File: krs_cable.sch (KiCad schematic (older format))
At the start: 0 parts

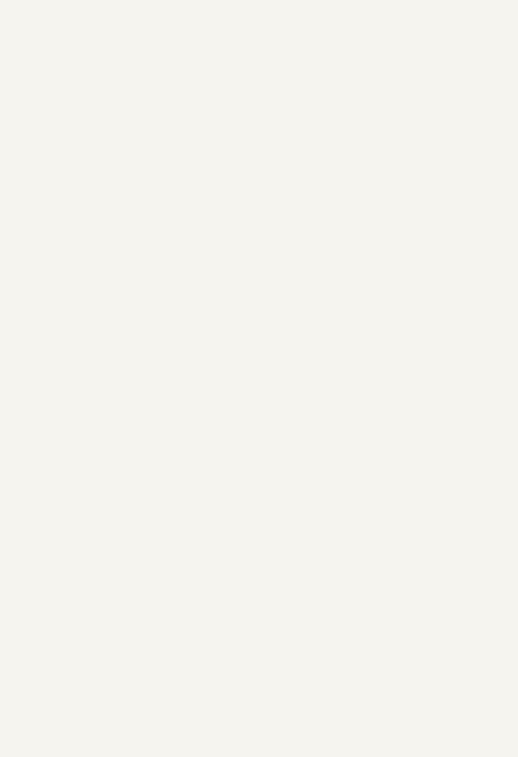
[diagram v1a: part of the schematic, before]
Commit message: set limits to pull down, optional invert
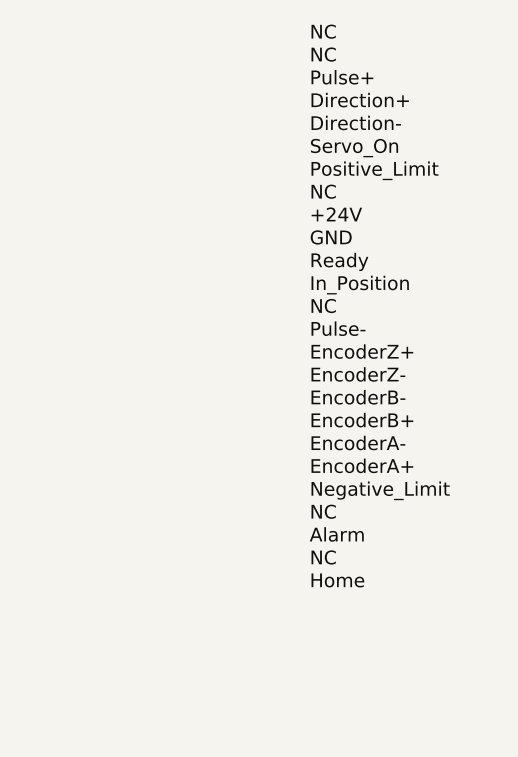
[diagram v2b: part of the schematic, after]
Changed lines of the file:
@@
 Text HLabel 4700 6500 3    60   Input ~ 0
 X2+24V
+Text Label 9000 1200 0    60   ~ 0
+NC
+Text Label 9000 1300 0    60   ~ 0
+NC
+Text Label 9000 1400 0    60   ~ 0
+Pulse+
+Text Label 9000 1500 0    60   ~ 0
+Direction+
+Text Label 9000 1600 0    60   ~ 0
+Direction-
+Text Label 9000 1700 0    60   ~ 0
+Servo_On
+Text Label 9000 1800 0    60   ~ 0
+Positive_Limit
+Text Label 9000 1900 0    60   ~ 0
+NC
+Text Label 9000 2000 0    60   ~ 0
++24V
+Text Label 9000 2100 0    60   ~ 0
+GND
+Text Label 9000 2200 0    60   ~ 0
+Ready
+Text Label 9000 2300 0    60   ~ 0
+In_Position
+Text Label 9000 2400 0    60   ~ 0
+NC
+Text Label 9000 2500 0    60   ~ 0
+Pulse-
+Text Label 9000 2600 0    60   ~ 0
+EncoderZ+
+Text Label 9000 2700 0    60   ~ 0
+EncoderZ-
+Text Label 9000 2800 0    60   ~ 0
+EncoderB-
+Text Label 9000 3000 0    60   ~ 0
+EncoderA-
+Text Label 9000 2900 0    60   ~ 0
+EncoderB+
+Text Label 9000 3100 0    60   ~ 0
+EncoderA+
+Text Label 9000 3200 0    60   ~ 0
+Negative_Limit
+Text Label 9000 3300 0    60   ~ 0
+NC
+Text Label 9000 3400 0    60   ~ 0
+Alarm
+Text Label 9000 3500 0    60   ~ 0
+NC
+Text Label 9000 3600 0    60   ~ 0
+Home
 $EndSCHEMATC

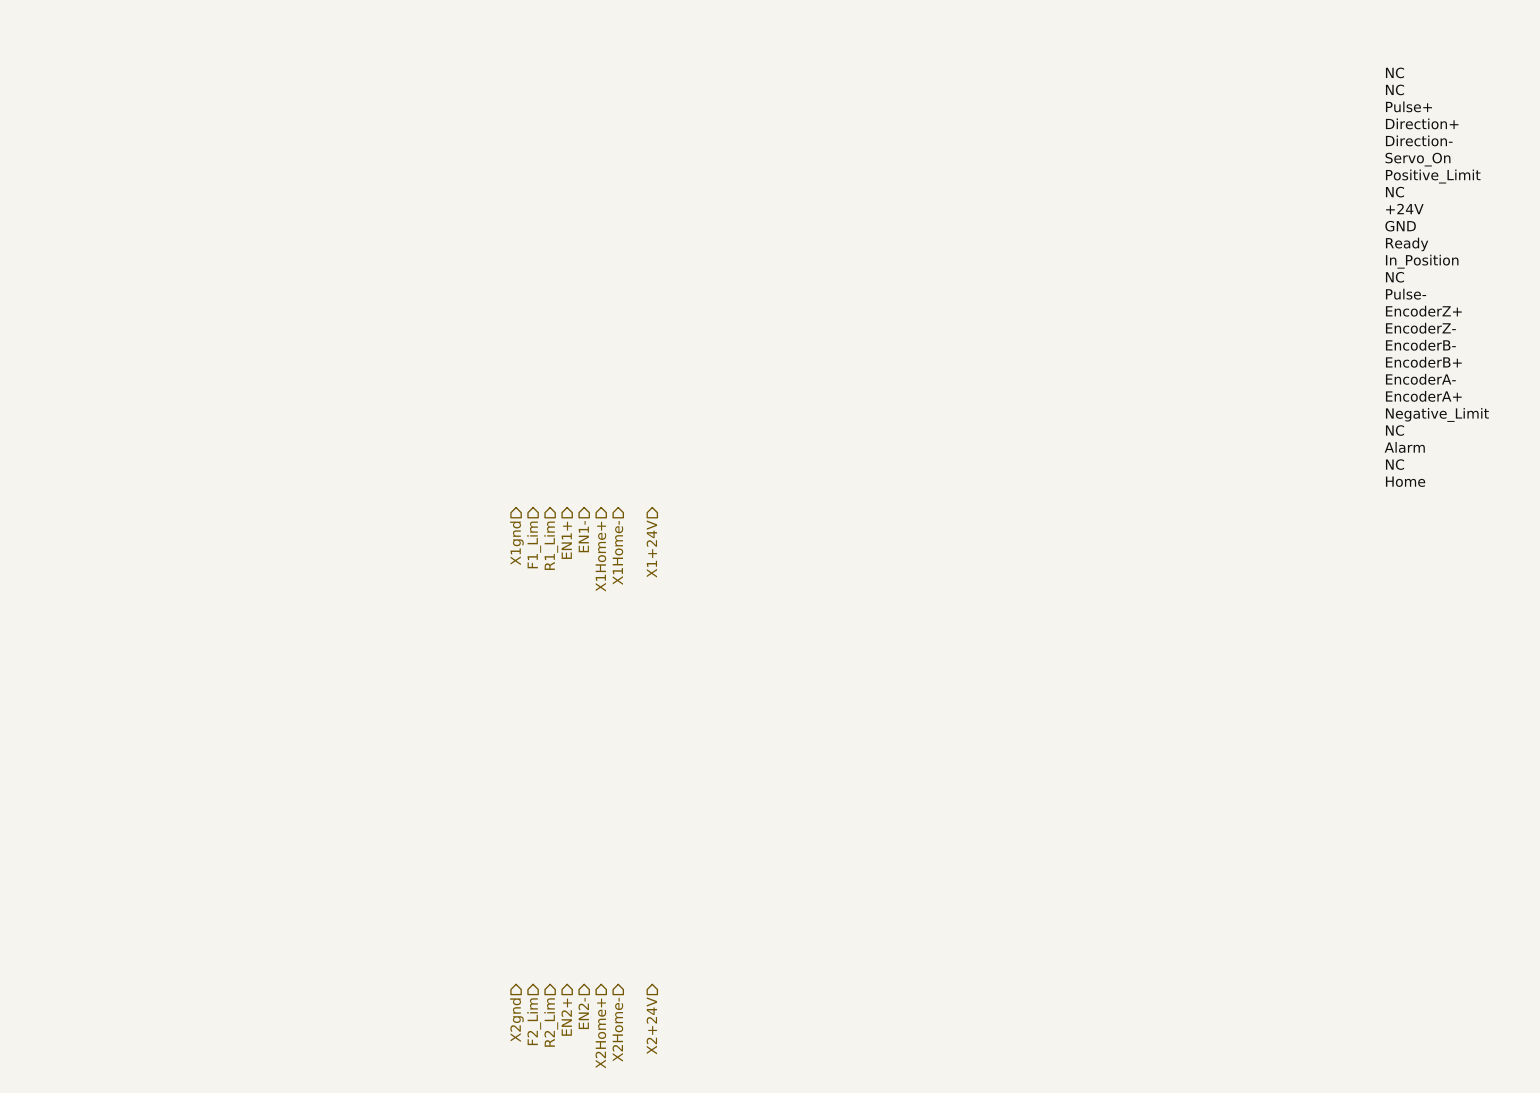
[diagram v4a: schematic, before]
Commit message: checked limits and homes, removed enable, adjusted routing
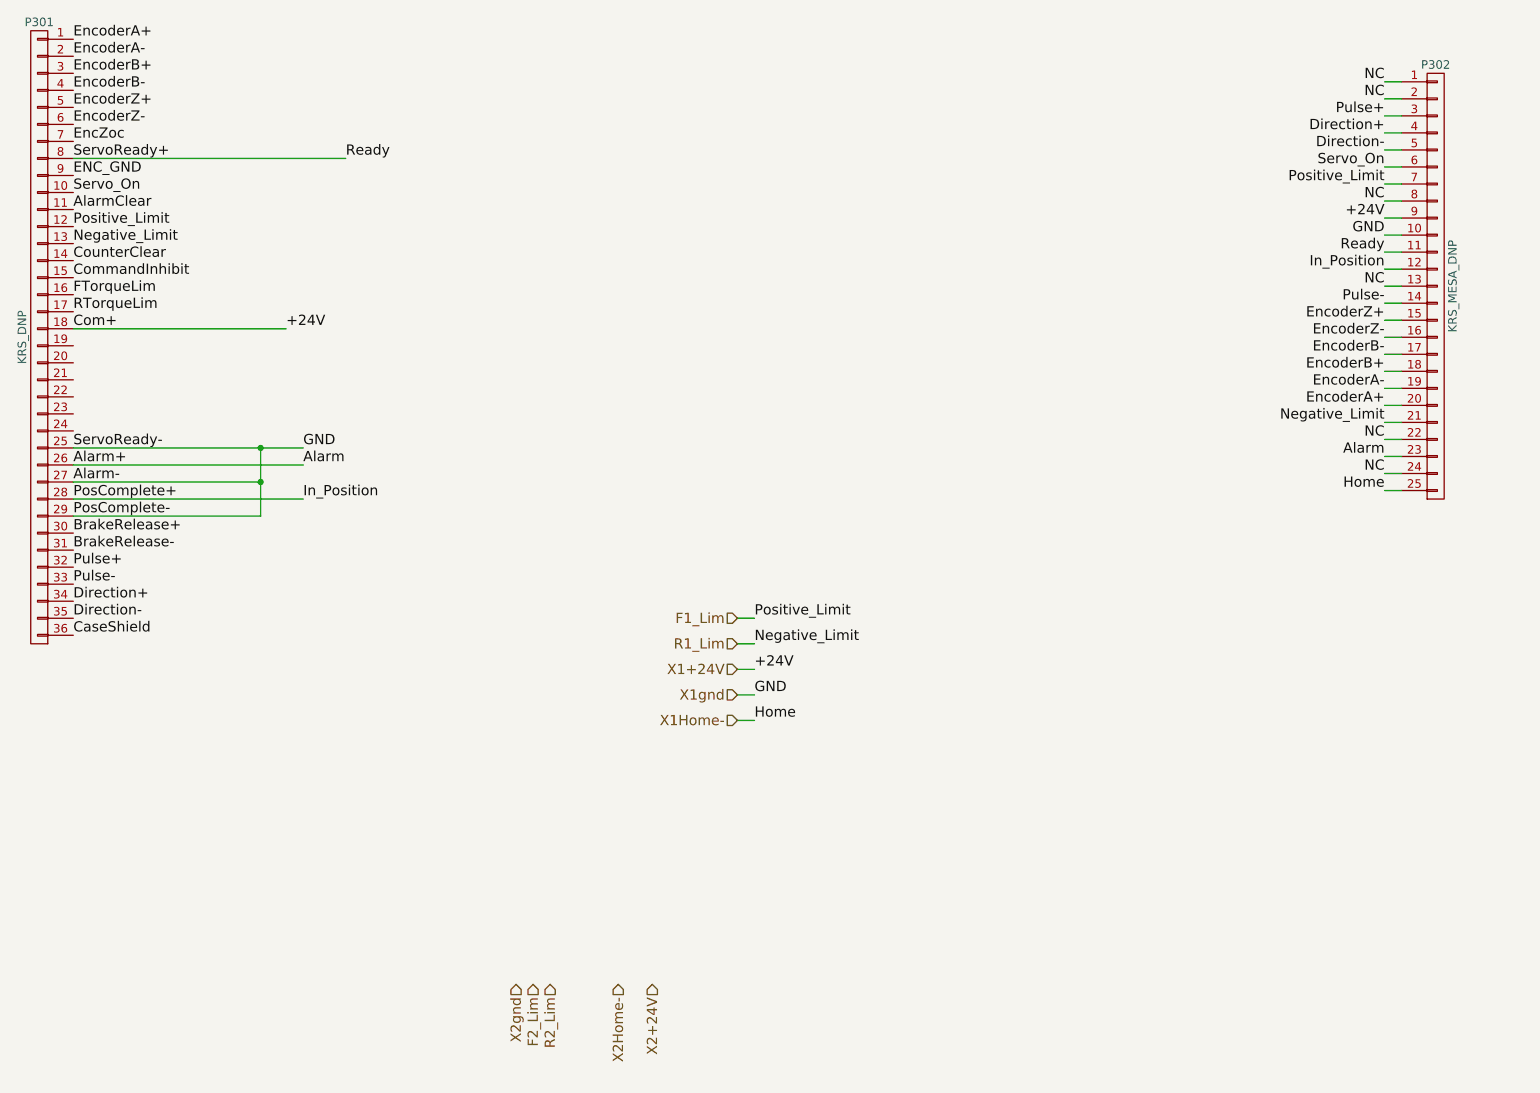
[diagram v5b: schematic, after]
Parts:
- added P301: KRS_DNP, symbol CONN_01X36
- added P302: KRS_MESA_DNP, symbol CONN_01X25
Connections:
- net Alarm: now also P301.26 (P26), P302.23 (P23)
- net Direction+: now also P301.34 (P34), P302.4 (P4)
- net Direction-: now also P301.35 (P35), P302.5 (P5)
- net EncoderA+: now also P301.1 (P1), P302.20 (P20)
- net EncoderA-: now also P301.2 (P2), P302.19 (P19)
- net EncoderB+: now also P301.3 (P3), P302.18 (P18)
- net EncoderB-: now also P301.4 (P4), P302.17 (P17)
- net EncoderZ+: now also P301.5 (P5), P302.15 (P15)
- net EncoderZ-: now also P301.6 (P6), P302.16 (P16)
- net F1_Lim: now also P301.12 (P12), P302.7 (P7)
- net In_Position: now also P301.28 (P28), P302.12 (P12)
- net NC: now also P302.1 (P1), P302.13 (P13), P302.2 (P2), P302.22 (P22), P302.24 (P24), P302.8 (P8)
- net Pulse+: now also P301.32 (P32), P302.3 (P3)
- net Pulse-: now also P301.33 (P33), P302.14 (P14)
- net R1_Lim: now also P301.13 (P13), P302.21 (P21)
- net Ready: now also P301.8 (P8), P302.11 (P11)
- net Servo_On: now also P301.10 (P10), P302.6 (P6)
- net X1+24V: now also P301.18 (P18), P302.9 (P9)
- net X1Home-: now also P302.25 (P25)
- net X1gnd: now also P301.25 (P25), P301.27 (P27), P301.29 (P29), P302.10 (P10)
- new net AlarmClear: P301.11 (P11)
- new net BrakeRelease+: P301.30 (P30)
- new net BrakeRelease-: P301.31 (P31)
- new net CaseShield: P301.36 (P36)
- new net CommandInhibit: P301.15 (P15)
- new net CounterClear: P301.14 (P14)
- new net ENC_GND: P301.9 (P9)
- new net EncZoc: P301.7 (P7)
- new net FTorqueLim: P301.16 (P16)
- new net RTorqueLim: P301.17 (P17)
